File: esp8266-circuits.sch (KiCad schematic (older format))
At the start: 14 parts

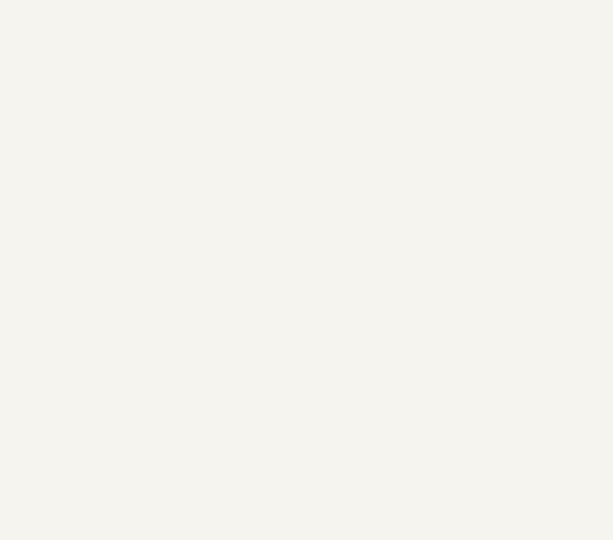
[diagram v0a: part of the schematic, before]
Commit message: battery level sensing added
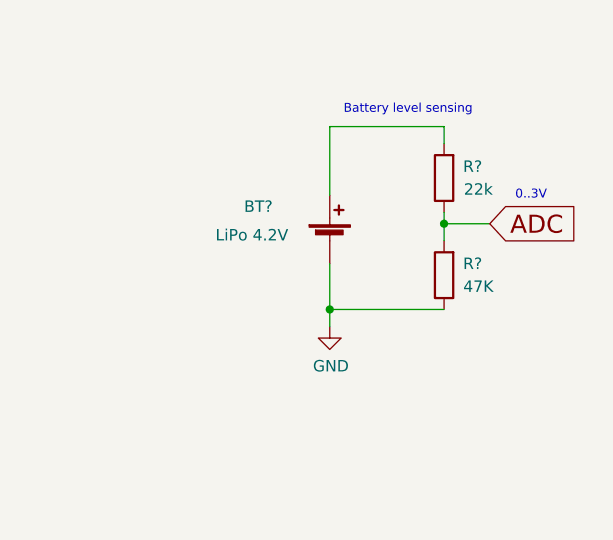
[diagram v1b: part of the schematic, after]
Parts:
- added BT?: LiPo 4.2V, symbol Device:Battery_Cell
- added R?: 22k, symbol Device:R
- added R?: 47K, symbol Device:R
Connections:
- net GND: now also BT?.2 (-), R?.1
- new net: BT?.1 (+), R?.2
- new net ADC: R?.1, R?.2
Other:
- note added: "0..3V"
- note added: "Battery level sensing"
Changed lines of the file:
@@
 Wire Wire Line
 	7900 2050 8100 2050
+$Comp
+L Device:Battery_Cell BT?
+U 1 1 5EC2839A
+P 11275 2300
+F 0 "BT?" H 10900 2450 50  0000 L CNN
+F 1 "LiPo 4.2V" H 10775 2325 50  0000 L CNN
+F 2 "" V 11275 2360 50  0001 C CNN
+F 3 "~" V 11275 2360 50  0001 C CNN
+	1    11275 2300
+	1    0    0    -1
+$EndComp
+$Comp
+L power:GND #PWR?
+U 1 1 5EC283A4
+P 11275 2675
+F 0 "#PWR?" H 11275 2425 50  0001 C CNN
+F 1 "GND" H 11280 2502 50  0000 C CNN
+F 2 "" H 11275 2675 50  0001 C CNN
+F 3 "" H 11275 2675 50  0001 C CNN
+	1    11275 2675
+	1    0    0    -1
+$EndComp
+Wire Wire Line
+	11275 1800 11275 2100
+$Comp
+L Device:R R?
+U 1 1 5EC2B473
+P 11775 2025
+F 0 "R?" H 11650 1975 50  0000 C CNN
+F 1 "22k" H 11625 2075 50  0000 C CNN
+F 2 "" V 11705 2025 50  0001 C CNN
+F 3 "~" H 11775 2025 50  0001 C CNN
+	1    11775 2025
+	-1   0    0    1
+$EndComp
+Wire Wire Line
+	11275 1800 11775 1800
+$Comp
+L Device:R R?
+U 1 1 5EC2D37D
+P 11775 2450
+F 0 "R?" H 11650 2400 50  0000 C CNN
+F 1 "47K" H 11625 2500 50  0000 C CNN
+F 2 "" V 11705 2450 50  0001 C CNN
+F 3 "~" H 11775 2450 50  0001 C CNN
+	1    11775 2450
+	-1   0    0    1
+$EndComp
+Wire Wire Line
+	11775 2600 11275 2600
+Wire Wire Line
+	11275 2400 11275 2600
+Connection ~ 11275 2600
+Wire Wire Line
+	11275 2600 11275 2675
+Wire Wire Line
+	11775 2175 11775 2225
+Wire Wire Line
+	11775 1800 11775 1875
+Wire Wire Line
+	11775 2225 11975 2225
+Connection ~ 11775 2225
+Wire Wire Line
+	11775 2225 11775 2300
+Text GLabel 11975 2225 2    79   Input ~ 0
+ADC
+Text Notes 12225 2125 2    39   ~ 0
+0..3V
+Text Notes 11900 1750 2    39   ~ 0
+Battery level sensing
 $EndSCHEMATC
